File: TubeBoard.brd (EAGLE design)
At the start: 63.5 x 60.6 mm, 11 parts, among them IC1 HV5530PQFP-44

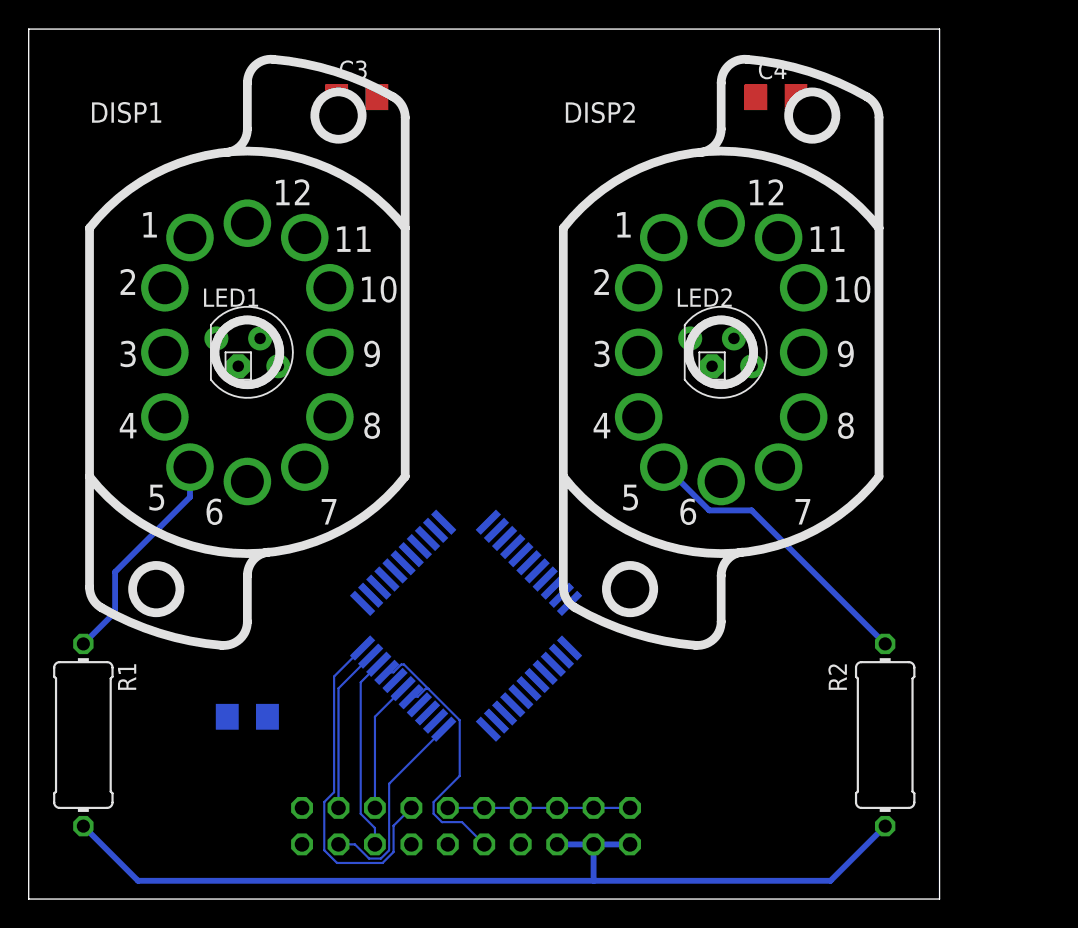
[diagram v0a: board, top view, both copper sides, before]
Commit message: Finished routing tube board
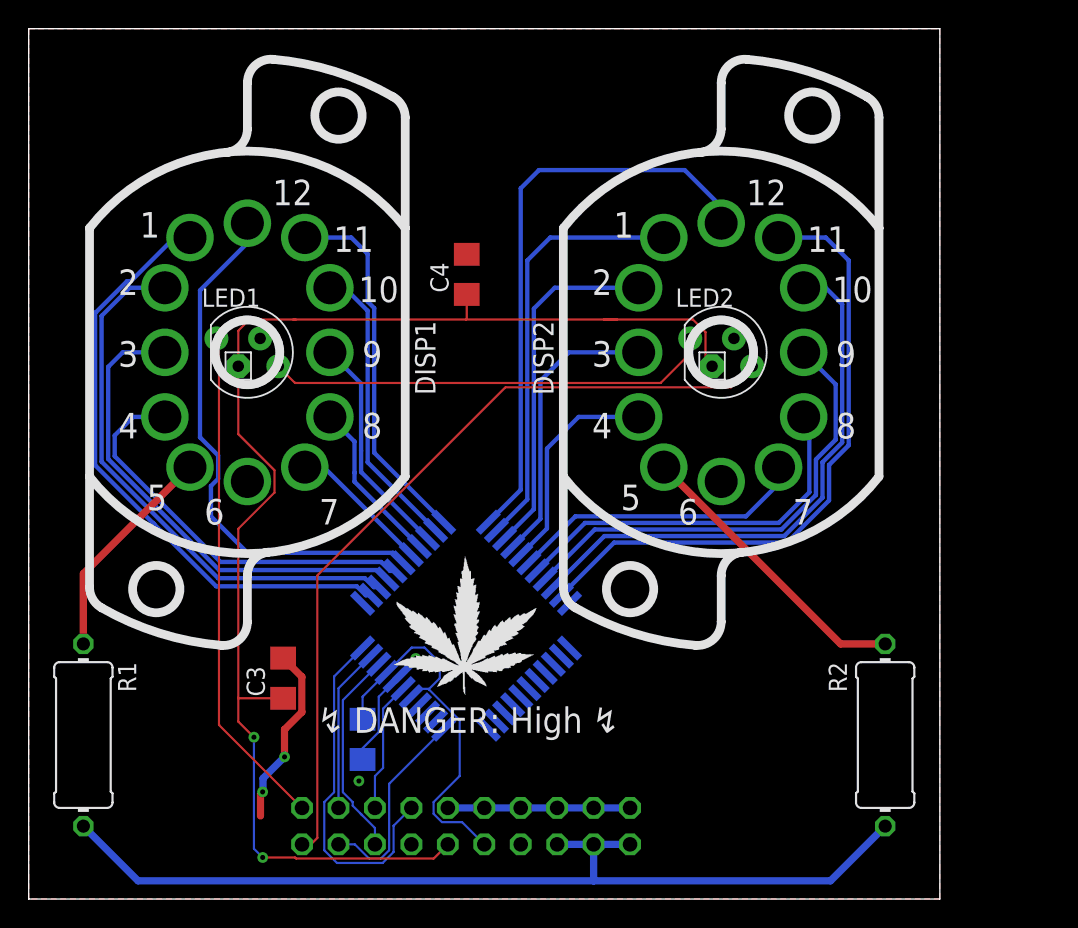
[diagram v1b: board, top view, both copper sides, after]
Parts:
- added WEED1: WEED, Parts:DOINK
- moved C3 40.8 mm to (17.7, 15.4), turned to 90 degrees
- moved C4 24.8 mm to (30.5, 43.5), turned to 90 degrees
- moved C1 8.18 mm to (23.3, 11.1), turned to 270 degrees
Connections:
- net 1_K0: now also IC1.38; no longer IC1.35
- net 1_K1: now also IC1.40; no longer IC1.36
- net 1_K2: now also IC1.41; no longer IC1.37
- net 1_K3: now also IC1.42; no longer IC1.38
- net 1_K4: now also IC1.43; no longer IC1.39
- net 1_K5: now also IC1.44; no longer IC1.40
- net 1_K6: now also IC1.39; no longer IC1.41
- net 1_K7: now also IC1.35; no longer IC1.42
- net 1_K8: now also IC1.36; no longer IC1.43
- net 1_K9: now also IC1.37; no longer IC1.44
- net 2_K0: now also IC1.5; no longer IC1.1
- net 2_K1: now also IC1.6; no longer IC1.2
- net 2_K2: now also IC1.7; no longer IC1.3
- net 2_K3: now also IC1.8; no longer IC1.4
- net 2_K4: now also IC1.9; no longer IC1.5
- net 2_K5: now also IC1.10; no longer IC1.6
- net 2_K6: now also IC1.1; no longer IC1.7
- net 2_K7: now also IC1.2; no longer IC1.8
- net 2_K8: now also IC1.3; no longer IC1.9
- net 2_K9: now also IC1.4; no longer IC1.10
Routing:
- net +5V: track 0.00 -> 94.6 mm, vias 0 -> 2
- net LED_DOUT: track 0.00 -> 55.9 mm
- net 2_K5: track 0.00 -> 44.2 mm
- net 1_K7: track 0.00 -> 42.6 mm
- net 2_K6: track 0.00 -> 40.9 mm
- net 2_K4: track 0.00 -> 38.6 mm
- net 1_K8: track 0.00 -> 38.3 mm
- net 1_K6: track 0.00 -> 37.3 mm
- net LED_DIN: track 0.00 -> 35.2 mm
- net 1_K9: track 0.00 -> 33.7 mm
- net 2_K3: track 0.00 -> 32.7 mm
- net LED_BUS: track 0.00 -> 31.1 mm
- net 2_K7: track 0.00 -> 29.9 mm
- net 1_K0: track 0.00 -> 28.3 mm
- net 2_K2: track 0.00 -> 26.7 mm
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- added copper zone on layer 1, net GND
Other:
- board size 63.5 x 60.6 mm -> 63.5 x 60.7 mm
- board text added: "IN-12A Serial Driver (c) 2018 Tristan Seifert"
- board text added: "↯ DANGER: High ↯"

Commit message: Added colons
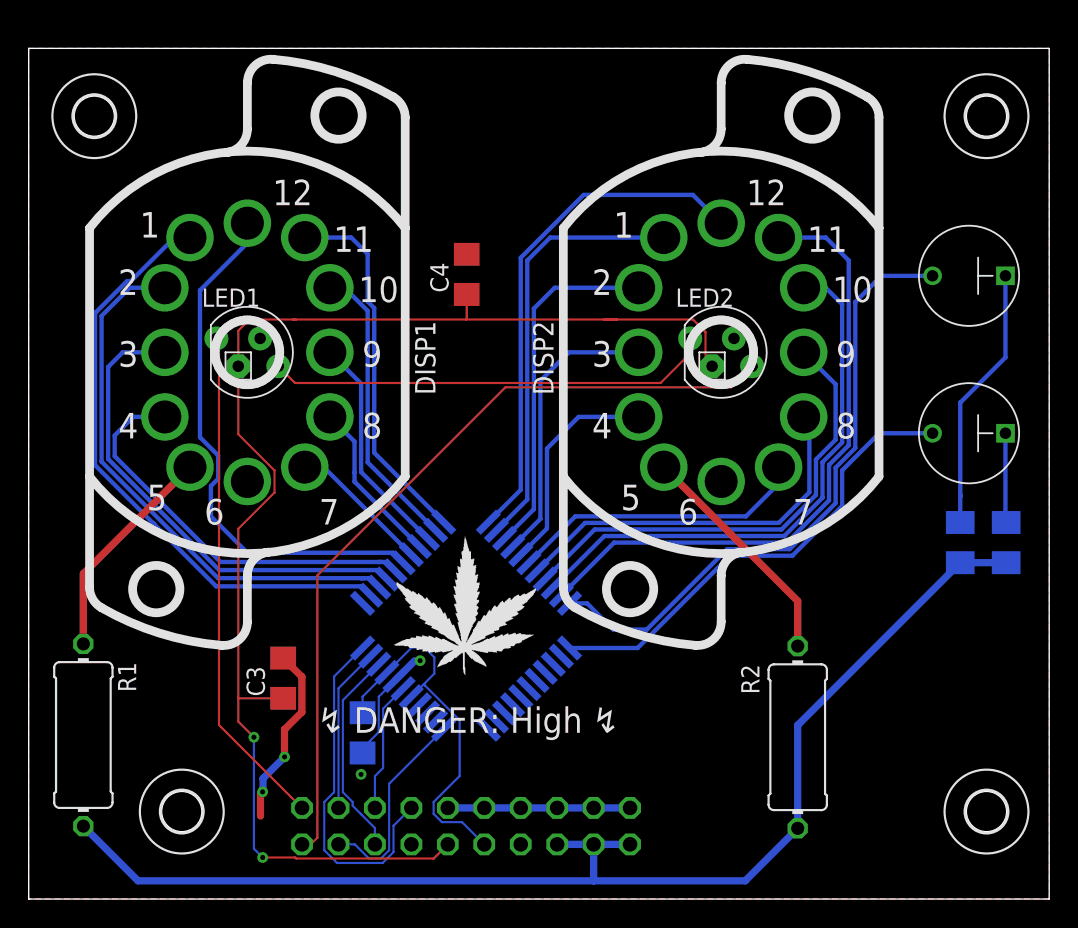
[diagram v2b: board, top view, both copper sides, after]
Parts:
- added H1, H2, H3, H4: MOUNT-HOLE2.8, holes:2,8
- added R3, R4: 174k, rcl:M1206
- added U$1, U$2: INS-1, Parts:INS-1
- moved R2 6.10 mm to (53.6, 11.3)
- moved WEED1 1.37 mm to (25.5, 15.5)
- moved C1 0.46 mm to (23.3, 11.6)
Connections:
- new net COLON_B: IC1.12, U$2.C
- new net COLON_T: IC1.11, U$1.C
- new net N$3: R3.2, U$1.A
- new net N$4: R4.2, U$2.A
- net HV_ANODE: now also R3.1, R4.1
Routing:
- net COLON_T: track 0.00 -> 43.7 mm
- net COLON_B: track 0.00 -> 32.9 mm
- net HV_ANODE: track 66.7 -> 88.1 mm
- net N$3: track 0.00 -> 18.6 mm
- net N$4: track 0.00 -> 6.24 mm
- net 2_K6: track 40.9 -> 36.0 mm
- net N$2: track 20.5 -> 16.3 mm
- net +12V: track 27.2 -> 26.5 mm
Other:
- board size 63.5 x 60.7 mm -> 71.1 x 59.3 mm
